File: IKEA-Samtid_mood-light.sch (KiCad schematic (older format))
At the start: 22 parts, among them IC1 ATMEGA168PA-M, P1 FTDI, P2 POWER, P3.1 B-to-B-1A, P3.2 B-to-B-1B, P4.1 B-to-B-2A, P4.2 B-to-B-2B, Q1 BSS138, Q2 BSS138, SW1 ENTER, SW2 MODE, X1 CSTCE16M0V53-R0

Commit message: Routed ADC2 to pin #2 of the FTDI connector.
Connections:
- net ADC2: now reaches P1.2
- net ADC2: now also IC1.25 ((PCINT10/ADC2)PC2)
- no-connect marks 27 -> 25
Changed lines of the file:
@@
 Title "IKEA-Samtid_mood-light"
 Date "26 Jul 2014"
-Rev "0.24"
+Rev "0.25"
 Comp "2014 - blog.spitzenpfeil.org"
 Comment1 ""
@@
 Text Label 1600 3750 2    60   ~ 0
 RST
-NoConn ~ 1900 2400
 Text Label 1800 2600 2    60   ~ 0
 RXI
@@
 NoConn ~ 5200 2700
 NoConn ~ 5200 2600
-NoConn ~ 5200 2500
 NoConn ~ 5200 2400
 NoConn ~ 5200 2300
@@
 Text Notes 2550 6350 0    39   ~ 0
 LED side\n5V > VCC.A
+Text Label 5300 2500 0    60   ~ 0
+ADC2
+Wire Wire Line
+	5200 2500 5300 2500
+Wire Wire Line
+	1900 2400 1800 2400
+Text Label 1800 2400 2    60   ~ 0
+ADC2
 $EndSCHEMATC

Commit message: Added a 100nF cap between DTR and RST ("auto-reset").
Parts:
- added C2: 100nF, symbol C
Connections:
- net RST: now also C2.1; no longer P1.6
- new net DTR: C2.2, P1.6

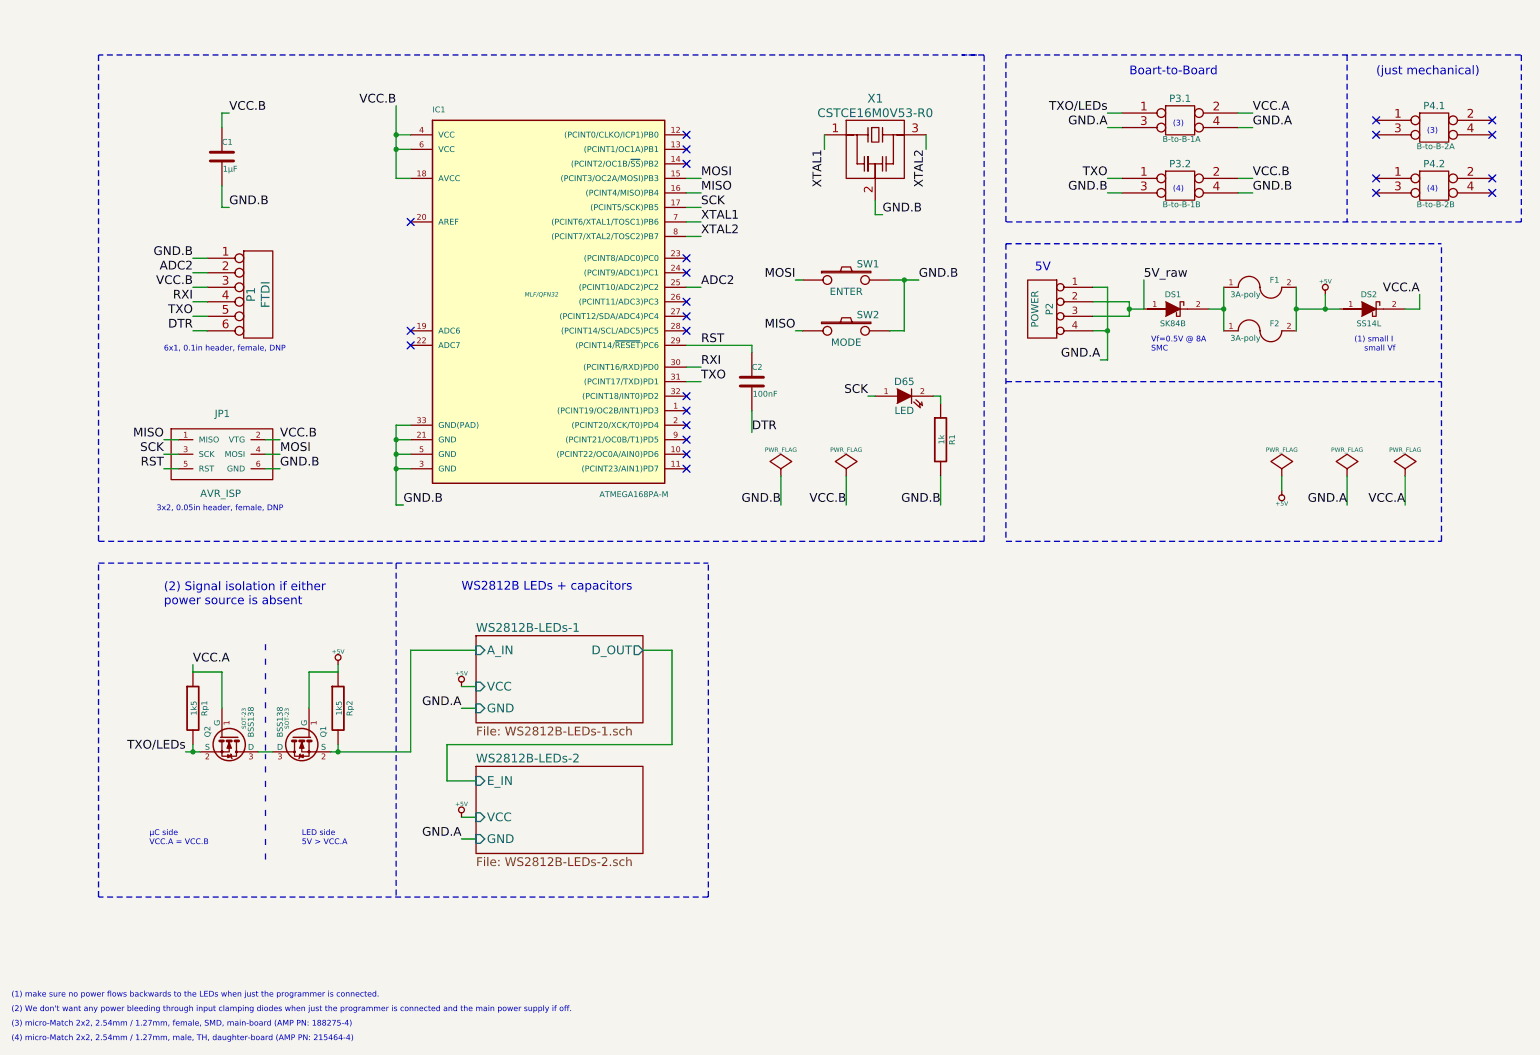
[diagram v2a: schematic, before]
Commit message: Had to split the project into two separate ones.
* LED board
* Control board

The PCB-fab doesn't like one layout with "board-in-board".
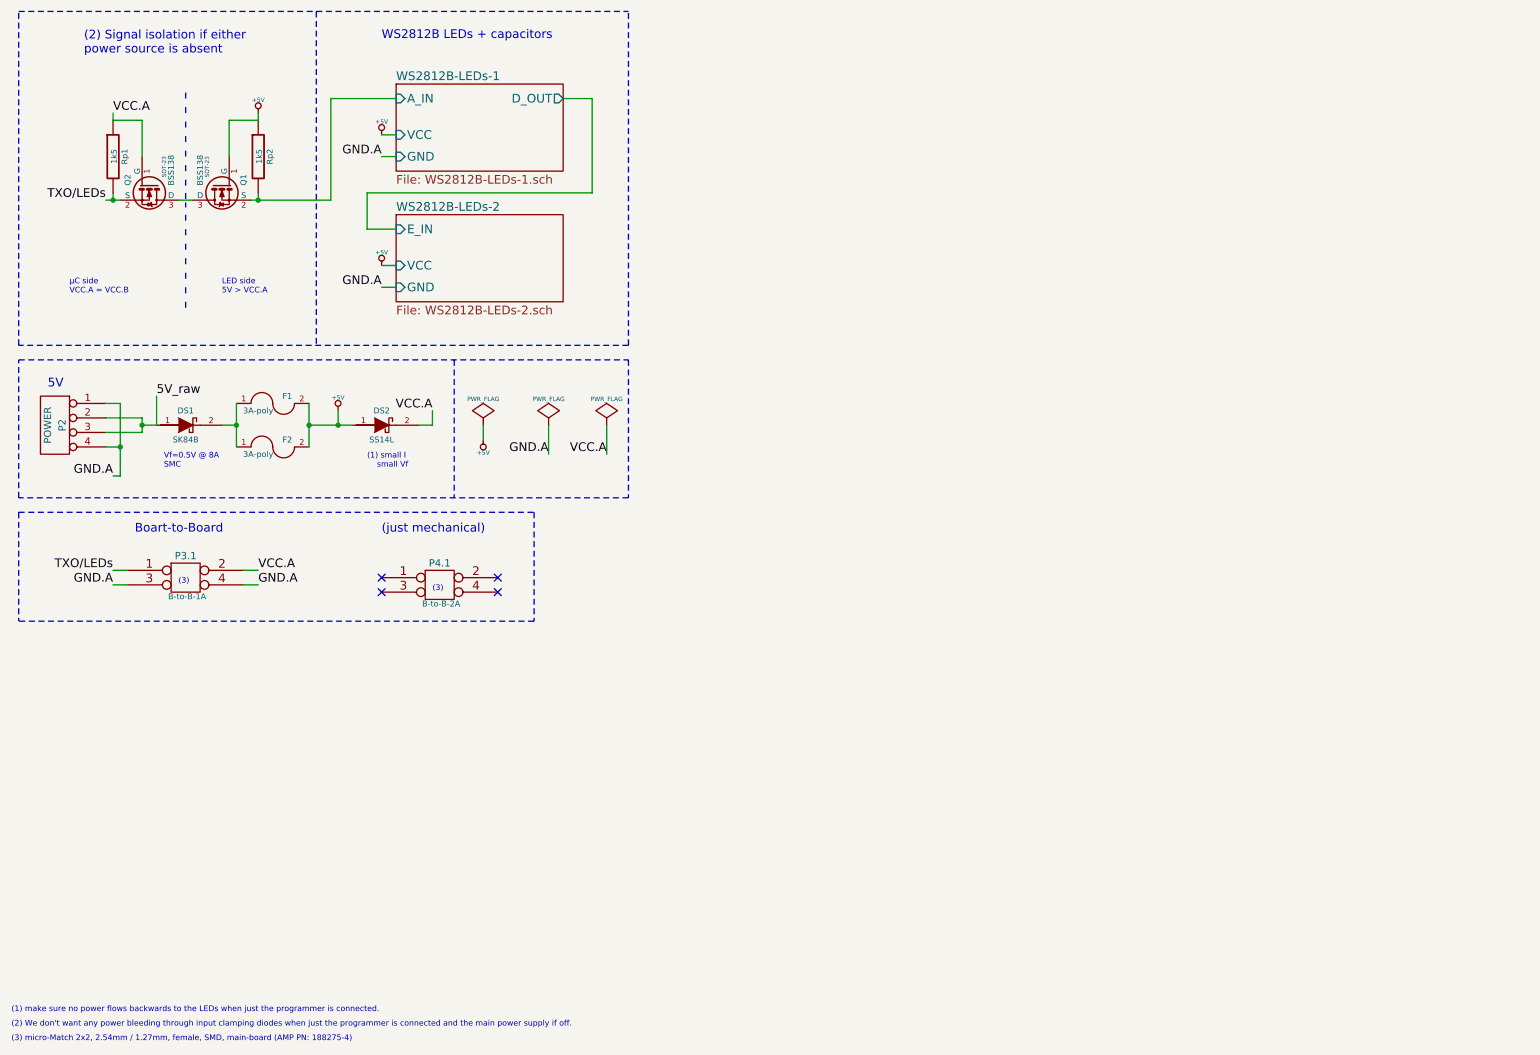
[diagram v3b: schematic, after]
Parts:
- removed C1: 1µF, symbol C
- removed C2: 100nF, symbol C
- removed D65: LED, symbol LED
- removed IC1: ATMEGA168PA-M, MLF/QFN32, symbol ATMEGA168PA-M
- removed JP1: AVR_ISP, symbol MADW__AVR_ISP
- removed P1: FTDI, symbol CONN_6
- removed P3.2: B-to-B-1B, symbol CONN_2X2
- removed P4.2: B-to-B-2B, symbol CONN_2X2
- removed R1: 1k, symbol R
- removed SW1: ENTER, symbol SW_PUSH
- removed SW2: MODE, symbol SW_PUSH
- removed X1: CSTCE16M0V53-R0, symbol generic_resonator
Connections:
- no-connect marks 25 -> 4
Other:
- note removed: "(4)"
- note removed: "(4) micro-Match 2x2, 2.54mm / 1.27mm, male, TH, daughter-board (AMP PN: 215464-4)"
- note removed: "3x2, 0.05in header, female, DNP"
- note removed: "6x1, 0.1in header, female, DNP"
- moved on the sheet: DS1, DS2, F1, F2, P2, P3.1, P4.1, Q1, Q2, Rp1, Rp2

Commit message: Went back to just 1 schematic file.
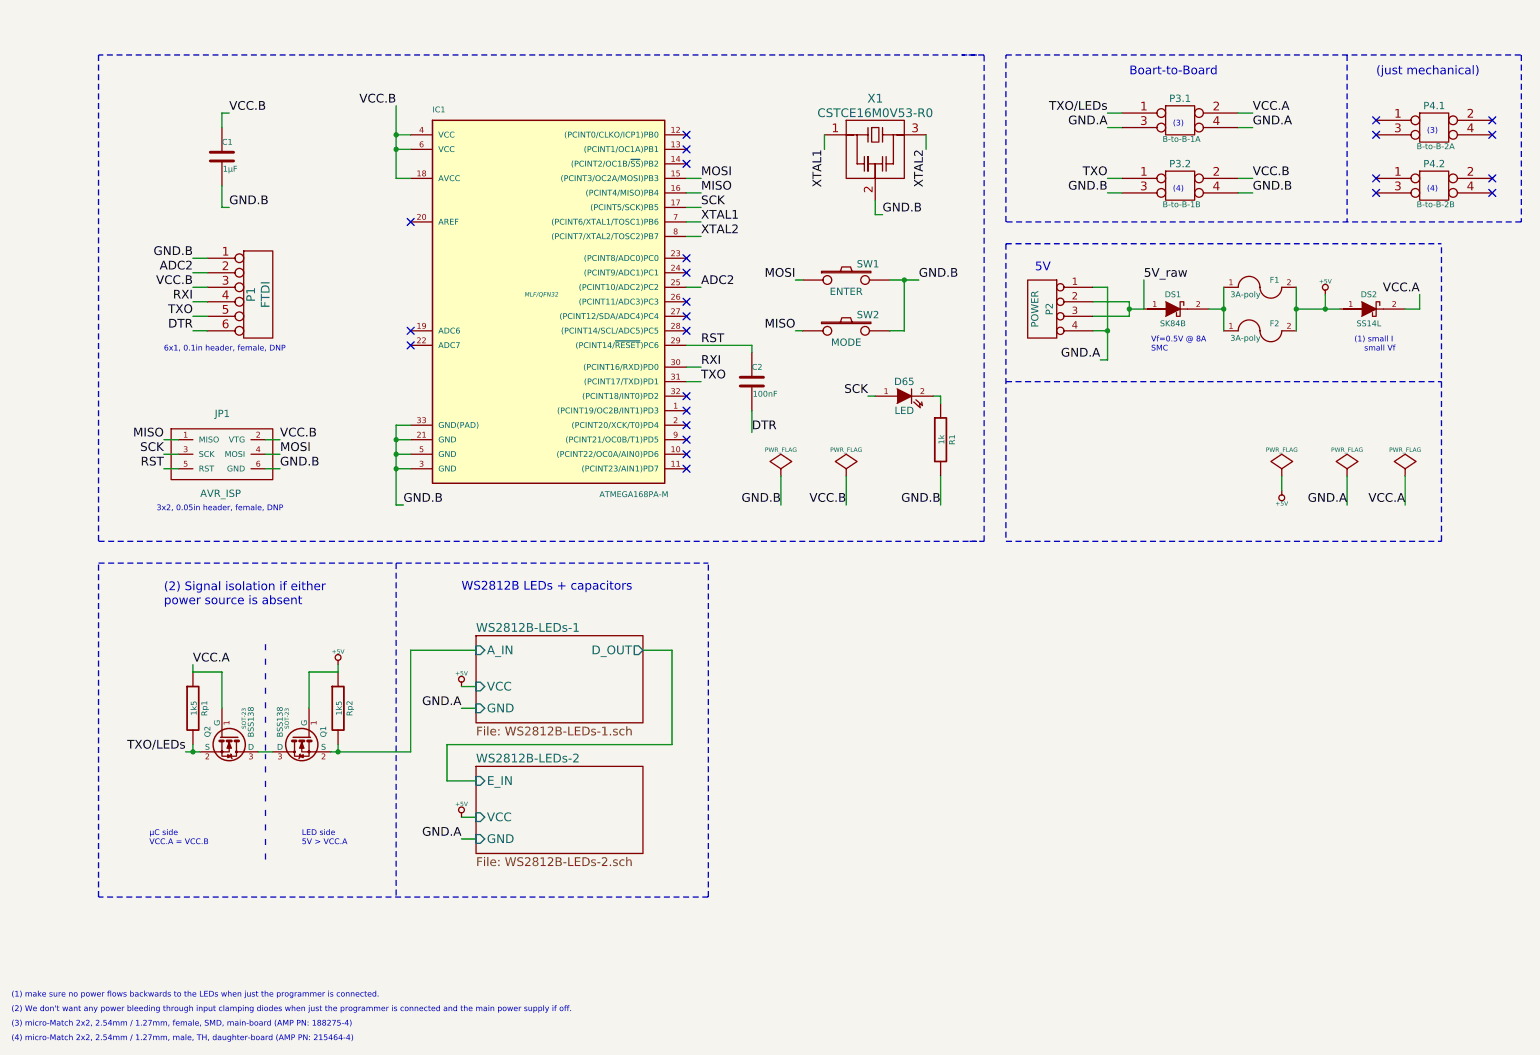
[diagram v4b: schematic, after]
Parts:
- added C1: 1µF, symbol C
- added C2: 100nF, symbol C
- added D65: LED, symbol LED
- added IC1: ATMEGA168PA-M, MLF/QFN32, symbol ATMEGA168PA-M
- added JP1: AVR_ISP, symbol MADW__AVR_ISP
- added P1: FTDI, symbol CONN_6
- added P3.2: B-to-B-1B, symbol CONN_2X2
- added P4.2: B-to-B-2B, symbol CONN_2X2
- added R1: 1k, symbol R
- added SW1: ENTER, symbol SW_PUSH
- added SW2: MODE, symbol SW_PUSH
- added X1: CSTCE16M0V53-R0, symbol generic_resonator
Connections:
- new net: D65.2 (K), R1.1
- new net ADC2: IC1.25 ((PCINT10/ADC2)PC2), P1.2
- new net DTR: C2.2, P1.6
- new net GND.B: C1.2, IC1.21 (GND), IC1.3 (GND), IC1.33 (GND(PAD)), IC1.5 (GND), JP1.6 (GND), P1.1, P3.2.3, P3.2.4, R1.2, SW1.2, SW2.2, X1.2
- new net MISO: IC1.16 ((PCINT4/MISO)PB4), JP1.1 (MISO), SW2.1
- new net MOSI: IC1.15 ((PCINT3/OC2A/MOSI)PB3), JP1.4 (MOSI), SW1.1
- new net RST: C2.1, IC1.29 ((PCINT14/~RESET~)PC6), JP1.5 (RST)
- new net RXI: IC1.30 ((PCINT16/RXD)PD0), P1.4
- new net SCK: D65.1 (A), IC1.17 ((PCINT5/SCK)PB5), JP1.3 (SCK)
- new net TXO: IC1.31 ((PCINT17/TXD)PD1), P1.5, P3.2.1
- new net VCC.B: C1.1, IC1.18 (AVCC), IC1.4 (VCC), IC1.6 (VCC), JP1.2 (VTG), P1.3, P3.2.2
- new net XTAL1: IC1.7 ((PCINT6/XTAL1/TOSC1)PB6), X1.1
- new net XTAL2: IC1.8 ((PCINT7/XTAL2/TOSC2)PB7), X1.3
- no-connect marks 4 -> 25
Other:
- note added: "(4)"
- note added: "(4) micro-Match 2x2, 2.54mm / 1.27mm, male, TH, daughter-board (AMP PN: 215464-4)"
- note added: "3x2, 0.05in header, female, DNP"
- note added: "6x1, 0.1in header, female, DNP"
- moved on the sheet: DS1, DS2, F1, F2, P2, P3.1, P4.1, Q1, Q2, Rp1, Rp2

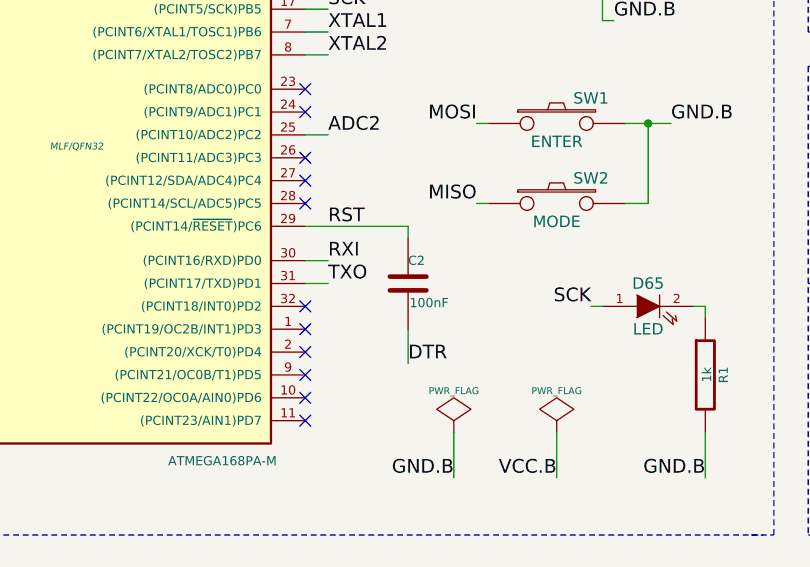
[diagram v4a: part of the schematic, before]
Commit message: Found & fixed auto-reset issue running 5V. 3.3V worked all the time.
Had to add 100k across the auto-reset capacitor C1.
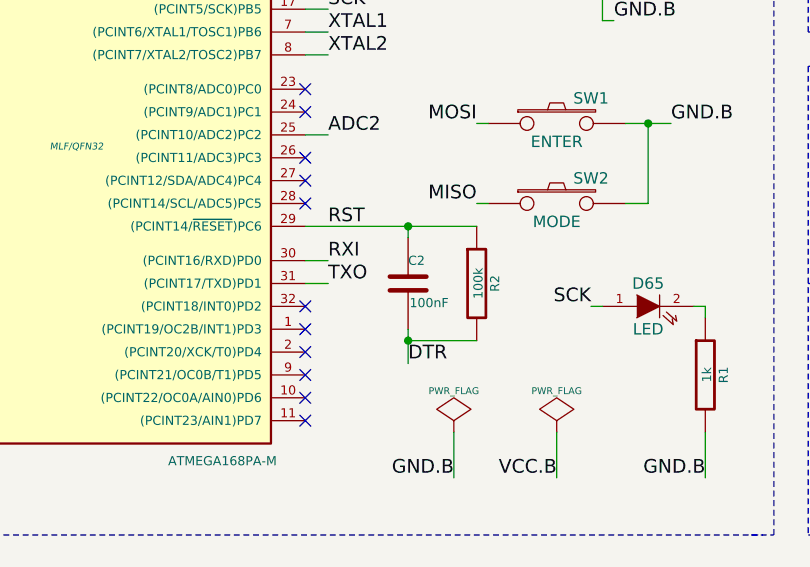
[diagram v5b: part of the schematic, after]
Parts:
- added R2: 100k, symbol R
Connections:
- net DTR: now also R2.2
- net RST: now also R2.1
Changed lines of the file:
@@
 LIBS:contrib
 LIBS:valves
+LIBS:IKEA-Samtid_mood-light-cache
 EELAYER 24 0
 EELAYER END
@@
 Sheet 1 3
 Title "IKEA-Samtid_mood-light"
-Date "04 Aug 2014"
-Rev "0.27"
+Date "23 Aug 2014"
+Rev "0.28"
 Comp "2014 - blog.spitzenpfeil.org"
 Comment1 ""
@@
 	6150 1450 6150 1550
 Wire Wire Line
-	5200 2900 5650 2900
+	5200 2900 5950 2900
 Wire Wire Line
 	6600 2450 6800 2450
@@
 Text Label 5300 2900 0    60   ~ 0
 RST
+$Comp
+L R R2
+U 1 1 53F8C068
+P 5950 3150
+F 0 "R2" V 6030 3150 40  0000 C CNN
+F 1 "100k" V 5957 3151 40  0000 C CNN
+F 2 "" V 5880 3150 30  0000 C CNN
+F 3 "" H 5950 3150 30  0000 C CNN
+	1    5950 3150
+	1    0    0    -1
+$EndComp
+Connection ~ 5650 2900
+Wire Wire Line
+	5650 3400 5950 3400
+Connection ~ 5650 3400
 $EndSCHEMATC
